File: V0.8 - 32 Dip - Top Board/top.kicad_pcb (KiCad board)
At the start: 4 copper layers, 18.5 x 41.7 mm, 21 parts, among them J1 Conn_01x02_Pin, J2 Conn_02x09_Counter_Clockwise, J3 Conn_01x20_Pin, J4 Conn_01x20_Pin, Q1 BC846, Q2 BSS84, Q3 BSS138, U1 M95P32-IXMNT/E, U2 AP2112K-3.3, U3 MCP23S17_SS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

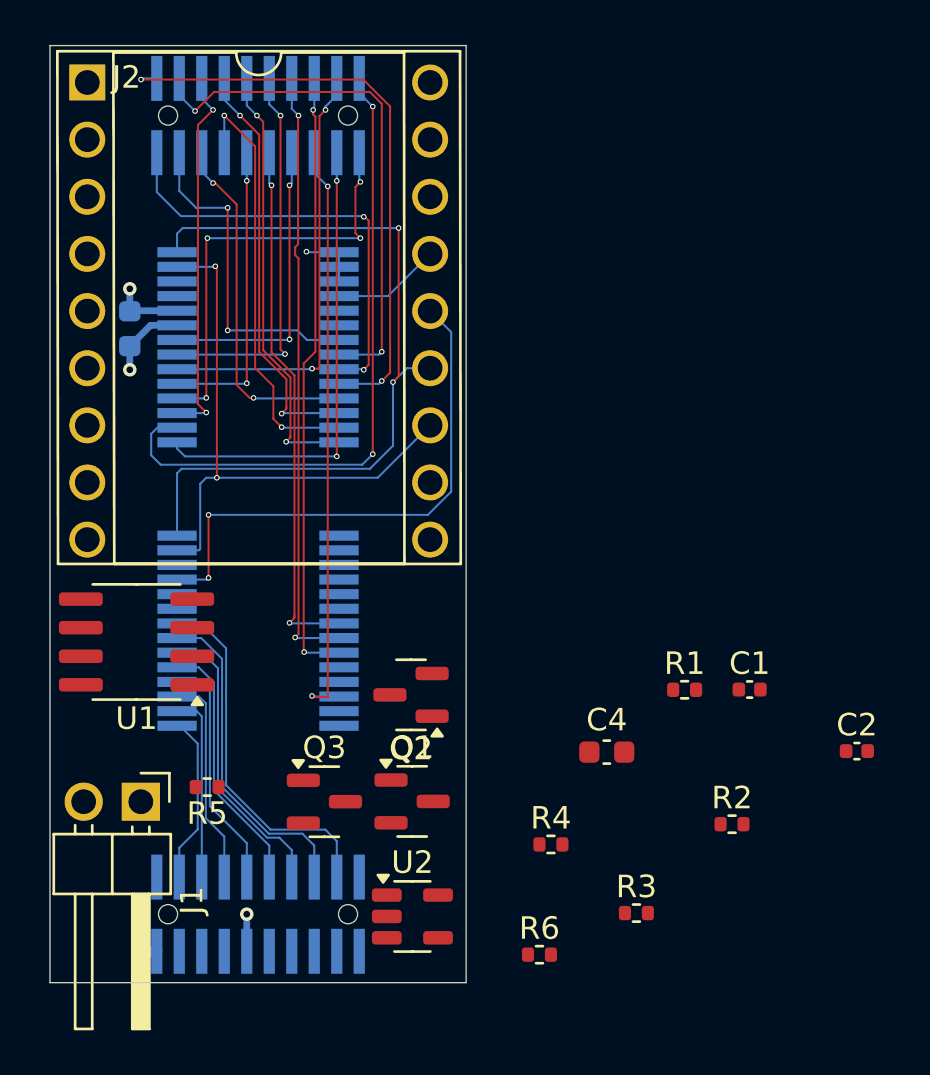
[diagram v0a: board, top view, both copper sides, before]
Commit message: Add Probe PCB, Latest Top/Bottom PCBs
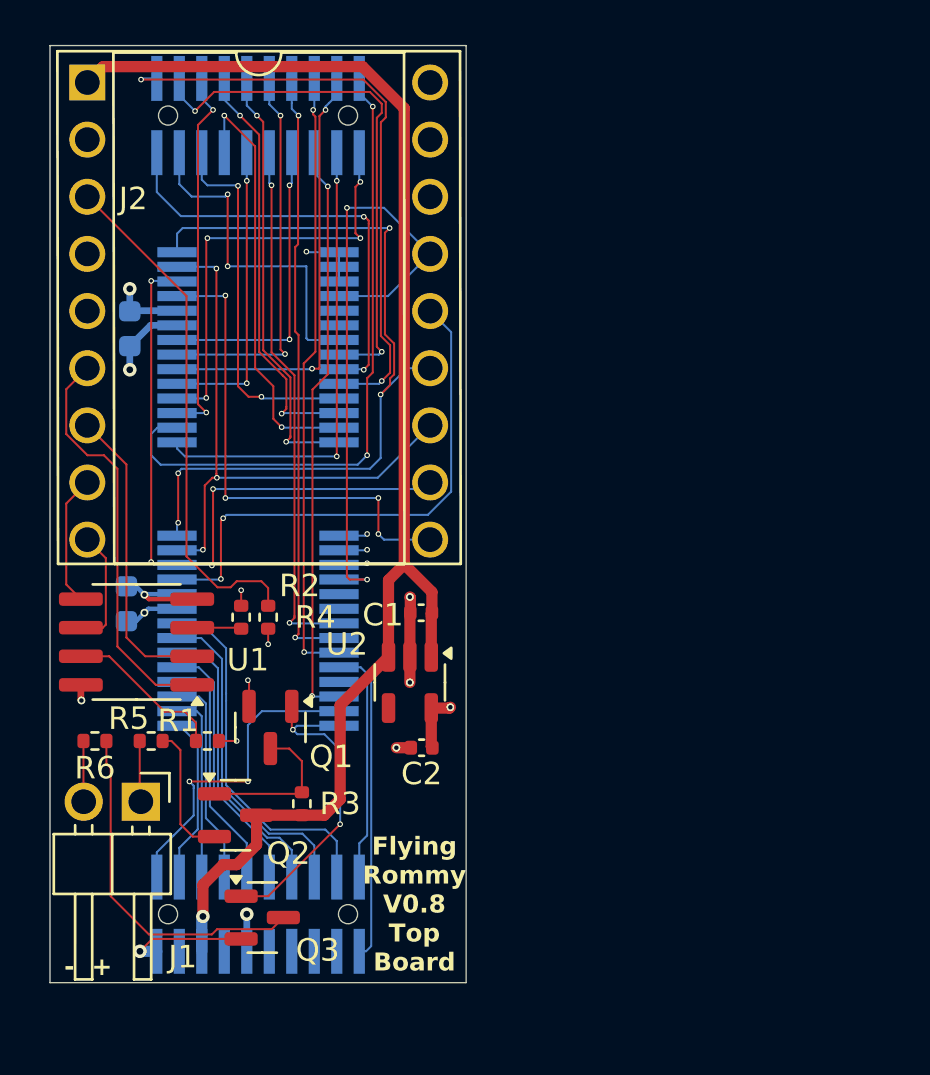
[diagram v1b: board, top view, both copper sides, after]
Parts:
- C4: moved to B.Cu
- moved R2 23.7 mm to (151.5, 107.2), turned to 90 degrees
- moved C4 22.3 mm to (146.4, 106.6), turned to 90 degrees
- moved R6 21.9 mm to (145.0, 112.7)
- moved R1 21.3 mm to (150.0, 112.7)
- moved C2 19.4 mm to (159.5, 113.0), turned to 180 degrees
- moved R4 16.1 mm to (152.7, 107.2), turned to 90 degrees
- moved R3 15.6 mm to (154.2, 115.5), turned to -90 degrees
- moved C1 15.0 mm to (159.5, 107.0), turned to 180 degrees
- moved U2 10.4 mm to (159.0, 110.1), turned to -90 degrees
- moved Q2 9.46 mm to (151.2, 116.0), turned to 0 degrees
- moved Q1 7.11 mm to (152.8, 112.1), turned to -90 degrees
- moved Q3 5.84 mm to (152.4, 120.5)
- moved R5 3.23 mm to (147.5, 112.7)
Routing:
- net /5v: track 0.00 -> 63.1 mm, vias 0 -> 1
- net Net-(J2-Pin_11): track 0.00 -> 29.6 mm, vias 0 -> 4
- net Net-(J2-Pin_15): track 4.83 -> 28.0 mm, vias 0 -> 2
- net Net-(J2-Pin_3): track 0.00 -> 23.0 mm
- net Net-(J2-Pin_10): track 0.00 -> 22.1 mm, vias 0 -> 4
- net Net-(J2-Pin_6): track 0.00 -> 18.2 mm
- net /GND: track 6.62 -> 24.2 mm, vias 3 -> 10
- net Net-(Q3-D): track 0.00 -> 15.7 mm
- net /Ext_Reset: track 0.00 -> 14.7 mm, vias 0 -> 2
- net /~{3v3-BusConnect}: track 0.00 -> 14.4 mm, vias 0 -> 2
- net /~{3v3-CE}: track 0.00 -> 14.2 mm
- net Net-(J2-Pin_7): track 0.00 -> 13.4 mm
- net /~{3v3-OE}: track 0.00 -> 10.00 mm
- net /3v3: track 5.18 -> 14.5 mm, vias 2 -> 9
- net Net-(U1-~{HOLD}): track 0.00 -> 7.15 mm
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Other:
- board text added: "- +"
- board text added: "Flying Rommy V0.8 Top Board"
